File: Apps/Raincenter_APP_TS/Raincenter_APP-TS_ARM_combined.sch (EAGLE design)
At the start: 31 parts, among them IC101 MAX232ECSE

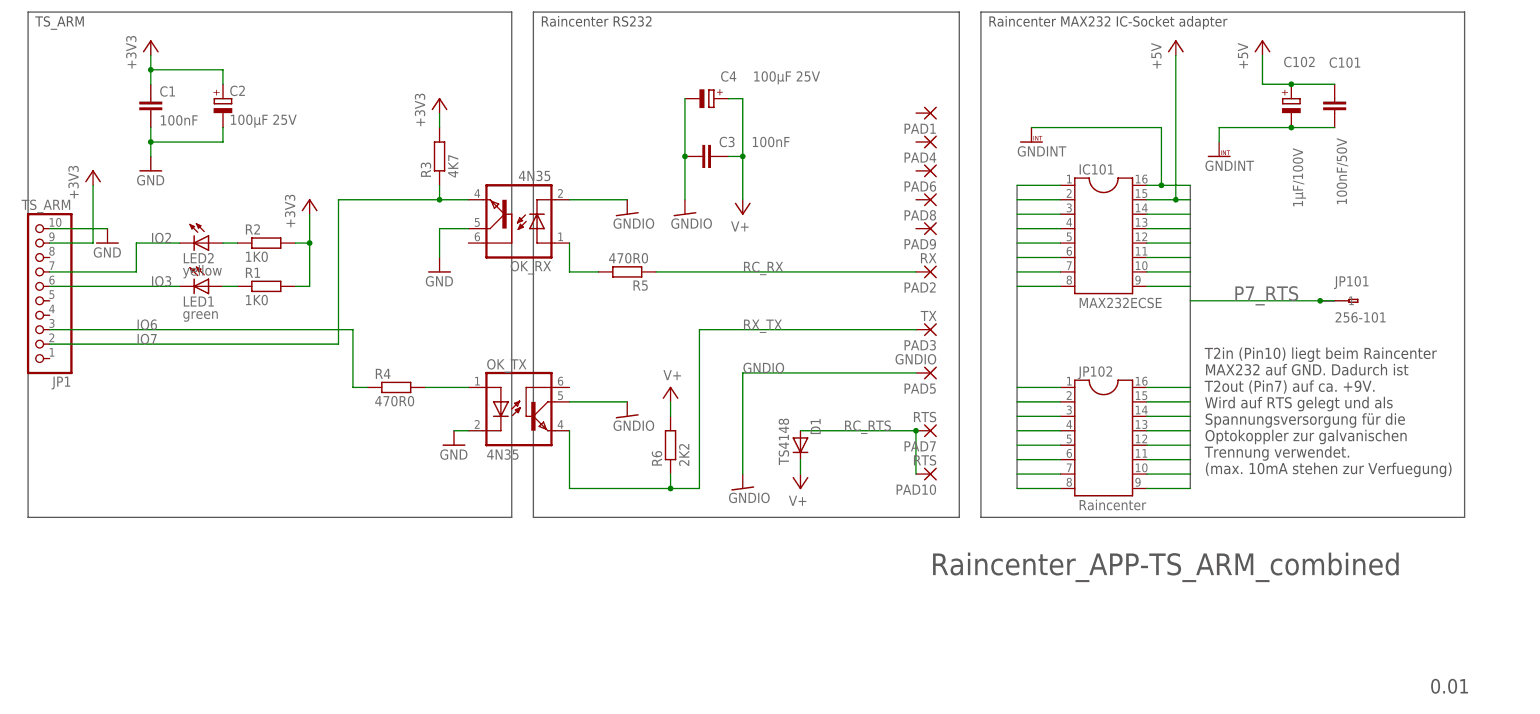
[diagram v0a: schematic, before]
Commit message: Raincenter_APP updated combinded schematic and board (for cheaper production) of Raincenter_APP_TS_ARM_ISO_0.02 & Raincenter_MAX232_Adapter_0.02
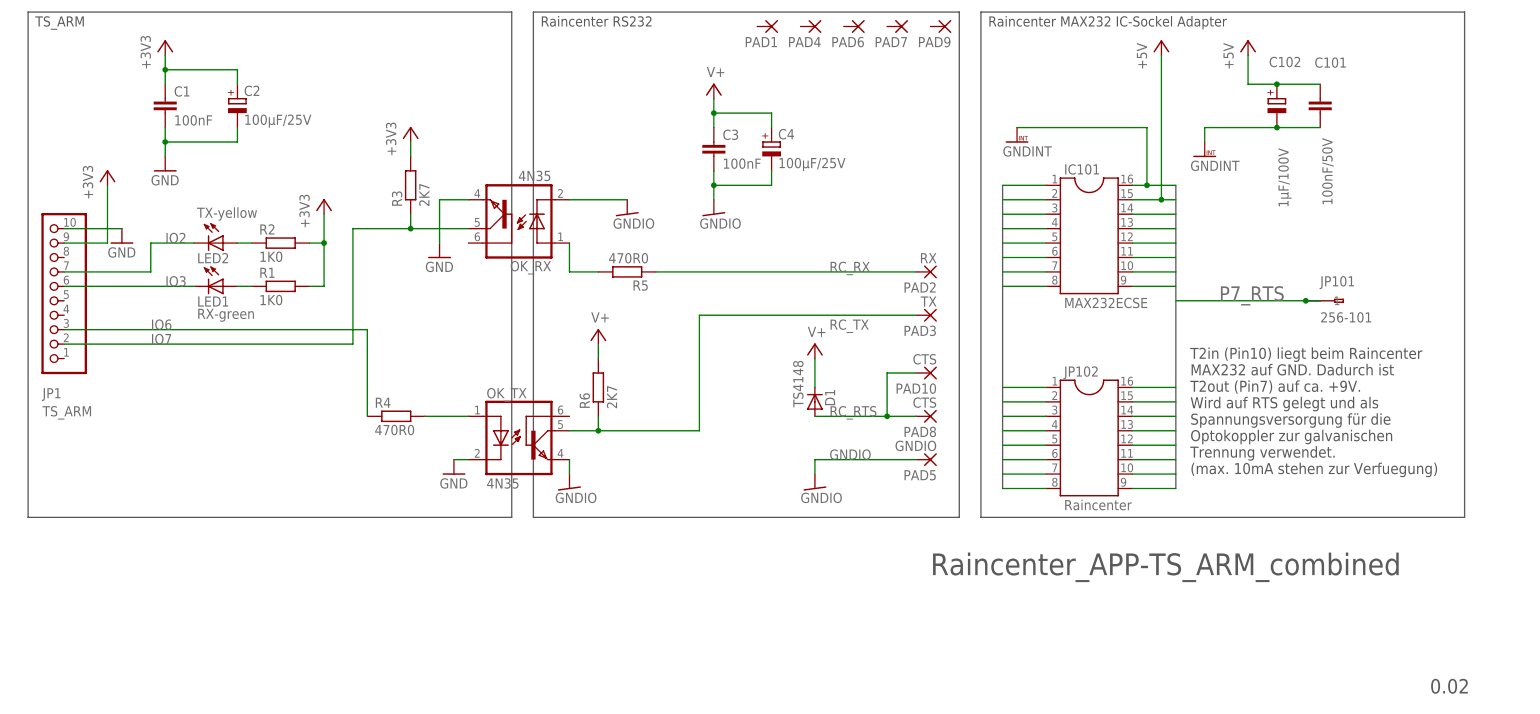
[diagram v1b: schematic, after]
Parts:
- C1, C3: OC_REICHELT (none) -> X7R-G1206 100N
- C101: OC_REICHELT (none) -> X7R-2,5 100N; REICHELT X7R-2,5 100N -> (none)
- C102: OC_REICHELT (none) -> RAD 105 1,0/100; REICHELT RAD 105 1,0/100 -> (none)
- C2, C4: value 100µF 25V -> 100µF/25V
- D1: OC_REICHELT (none) -> TS 4148-1206
- IC101: OC_REICHELT (none) -> GS 16P; REICHELT GS 16P -> (none)
- JP102: OC_REICHELT (none) -> AR 16; REICHELT AR 16 -> (none)
- LED1: value green -> RX-green; OC_REICHELT (none) -> SMD-LED 1206 GN; REICHELT SMD-LED 1206 GN -> (none)
- LED2: value yellow -> TX-yellow; OC_REICHELT (none) -> SMD-LED 1206 GE; REICHELT SMD-LED 1206 GE -> (none)
- OK_RX, OK_TX: OC_REICHELT (none) -> 4N 35
- PAD10: value RTS -> CTS
- PAD7: value RTS -> WIREPADSMD1,27-254
- PAD8: value WIREPADSMD1,27-254 -> CTS
- R1, R2: OC_REICHELT (none) -> RND 1206 1 1,0K; REICHELT RND 1206 1 1,0K -> (none)
- R3: value 4K7 -> 2K7; OC_REICHELT (none) -> RND 1206 1 2,7K; REICHELT RND 1206 1 4,7K -> (none)
- R4, R5: OC_REICHELT (none) -> RND 1206 1 470; REICHELT RND 1206 1 470 -> (none)
- R6: value 2K2 -> 2K7; OC_REICHELT (none) -> RND 1206 1 2,7K; REICHELT RND 1206 1 3,9K -> (none)
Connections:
- removed net RX_TX: OK_TX.EMI, PAD3.P, R6.1
- new net RC_TX: OK_TX.COL, PAD3.P, R6.1
- net GND: now also OK_RX.EMI; no longer OK_RX.COL
- net GNDIO: now also OK_TX.EMI; no longer OK_TX.COL
- net IO7: now also OK_RX.COL; no longer OK_RX.EMI
- net RC_RTS: now also PAD8.P; no longer PAD7.P
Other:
- note added: "0.02"
- note added: "Raincenter MAX232 IC-Sockel Adapter"
- note removed: "0.01"
- note removed: "Raincenter MAX232 IC-Socket adapter"
- moved on the sheet: C1, C101, C102, C2, C3, C4, D1, IC101, JP1, JP101, JP102, LED1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
